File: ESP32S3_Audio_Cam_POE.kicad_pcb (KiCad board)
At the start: 4 copper layers, 109.2 x 129.5 mm, 398 parts, among them J1 Connector, USB-TYPE-C-16P, J10 Conn_01x02, J11 Conn_01x02, J12 Conn_01x02, J13 Conn_01x02, J14 Conn_01x02, J15 Conn_01x02, J16 Conn_01x02, J17 Conn_01x02, J18 Conn_01x02, J19 Conn_01x02, J2 Connector, USB-TYPE-C-16P, J3 Conn_01x02, J4 Conn_01x02, J5 Conn_01x03, J6 Conn_01x03, J7 Conn_01x03, J8 Conn_01x03, J9 HC-RJ45-055-4_8P8C_Shielded, Q1 AO3401A, Q2 AO3401A, Q3 AO3401A, Q4 AO3401A, Q5 AO3401A, Q6 AO3401A, Q7 AO3401A, Q8 AO3401A, T1 H1102NLT, U1 TLV62568DBVR, U10 W25Q128JVSIQ, U11 TM1637, U12 DS18B20U(UMW), U13 W25Q128JVSIQ, U14 DP9900M-5V, U15 MAX98357AETE+T, U16 ICS-43434, U17 ICS-43434, U18 AXP2101, U2 MT9221CT-06BR5, U3 USBLC6-2SC6, U4 USBLC6-2SC6, U5 XC6206-1.5NR, U6 XC6206-2.8V, U7 ESP32-S3, U8 ESP32-S3, U9 W5500, X1 X322525MOB4SI, Y1 40MHz, 15pF, Y2 40MHz, 15pF, Y3 32.768KHz

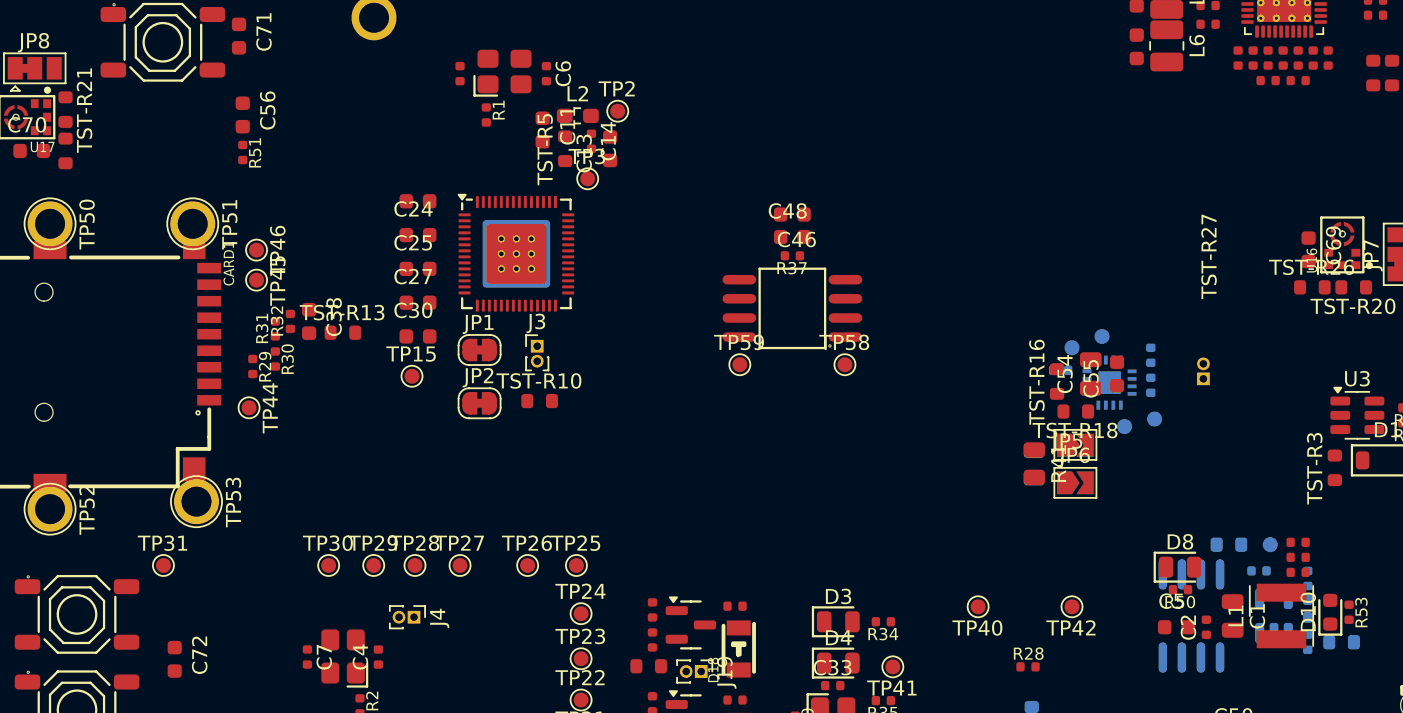
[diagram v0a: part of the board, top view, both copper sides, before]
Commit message: DRAFT added mic jack.
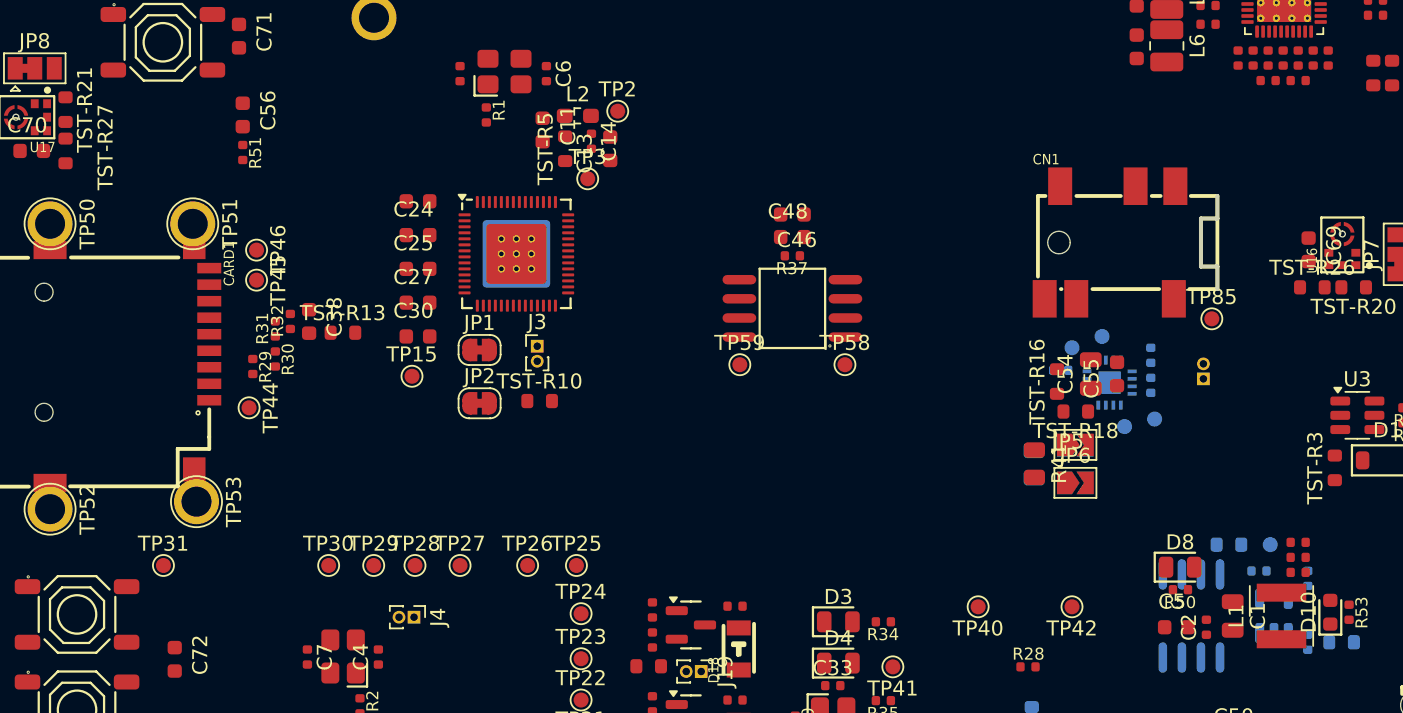
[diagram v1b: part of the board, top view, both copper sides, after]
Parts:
- removed the R8 at (133.4, 113.9)
- added CN1: PJ-316C-6A, JLCPCB:SMD_3.5mm_Audio_Connectors_(Headphones)_C707223, F.Cu at (120.2, 89.5)
- added TP85: TestPoint, TestPoint:TestPoint_Pad_D1.0mm, F.Cu at (127.0, 94.6)
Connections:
- C66 pad 2: Net-(J10-Pin_1) -> /SPK.OutN
- C67 pad 1: Net-(J10-Pin_2) -> /SPK.OutP
- J10 pad 1: Net-(J10-Pin_1) -> /SPK.OutPS
- J10 pad 2: Net-(J10-Pin_2) -> /SPK.OutN
- U15 pad 10: Net-(J10-Pin_1) -> /SPK.OutN
- U15 pad 9: Net-(J10-Pin_2) -> /SPK.OutP

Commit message: Draft Misc changes, layout still needs a lot of work.
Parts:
- added TP100: TestPoint, Connector_PinHeader_1.00mm:PinHeader_1x01_P1.00mm_Vertical, F.Cu at (71.8, 66.3)
- added TP101: TestPoint, Connector_PinHeader_1.00mm:PinHeader_1x01_P1.00mm_Vertical, F.Cu at (72.9, 66.3)
- added TP102: TestPoint, Connector_PinHeader_1.00mm:PinHeader_1x01_P1.00mm_Vertical, F.Cu at (74.1, 65.8)
- added TP103: TestPoint, Connector_PinHeader_1.00mm:PinHeader_1x01_P1.00mm_Vertical, F.Cu at (75.1, 65.8)
- added TP104: TestPoint, Connector_PinHeader_1.00mm:PinHeader_1x01_P1.00mm_Vertical, F.Cu at (76.2, 65.5)
- added TP105: TestPoint, Connector_PinHeader_1.00mm:PinHeader_1x01_P1.00mm_Vertical, F.Cu at (77.3, 65.5)
- added TP106: TestPoint, Connector_PinHeader_1.00mm:PinHeader_1x01_P1.00mm_Vertical, F.Cu at (66.4, 65.0)
- added TP107: TestPoint, Connector_PinHeader_1.00mm:PinHeader_1x01_P1.00mm_Vertical, F.Cu at (65.3, 65.0)
- added TP108: TestPoint, Connector_PinHeader_1.00mm:PinHeader_1x01_P1.00mm_Vertical, F.Cu at (68.6, 64.4)
- added TP109: TestPoint, Connector_PinHeader_1.00mm:PinHeader_1x01_P1.00mm_Vertical, F.Cu at (67.5, 64.4)
- added TP110: TestPoint, Connector_PinHeader_1.00mm:PinHeader_1x01_P1.00mm_Vertical, F.Cu at (70.8, 63.9)
- added TP111: TestPoint, Connector_PinHeader_1.00mm:PinHeader_1x01_P1.00mm_Vertical, F.Cu at (69.8, 63.9)
- added TP112: TestPoint, Connector_PinHeader_1.00mm:PinHeader_1x01_P1.00mm_Vertical, F.Cu at (73.0, 63.4)
- added TP113: TestPoint, Connector_PinHeader_1.00mm:PinHeader_1x01_P1.00mm_Vertical, F.Cu at (71.9, 63.4)
- added TP114: TestPoint, Connector_PinHeader_1.00mm:PinHeader_1x01_P1.00mm_Vertical, F.Cu at (75.1, 62.9)
- added TP115: TestPoint, Connector_PinHeader_1.00mm:PinHeader_1x01_P1.00mm_Vertical, F.Cu at (74.1, 62.9)
- added TP116: TestPoint, Connector_PinHeader_1.00mm:PinHeader_1x01_P1.00mm_Vertical, F.Cu at (77.3, 62.4)
- added TP117: TestPoint, Connector_PinHeader_1.00mm:PinHeader_1x01_P1.00mm_Vertical, F.Cu at (76.3, 62.4)
- added TP118: TestPoint, Connector_PinHeader_1.00mm:PinHeader_1x01_P1.00mm_Vertical, F.Cu at (66.5, 61.8)
- added TP119: TestPoint, Connector_PinHeader_1.00mm:PinHeader_1x01_P1.00mm_Vertical, F.Cu at (65.5, 61.8)
- added TP120: TestPoint, Connector_PinHeader_1.00mm:PinHeader_1x01_P1.00mm_Vertical, F.Cu at (68.6, 61.3)
- added TP121: TestPoint, Connector_PinHeader_1.00mm:PinHeader_1x01_P1.00mm_Vertical, F.Cu at (67.6, 61.3)
- added TP122: TestPoint, Connector_PinHeader_1.00mm:PinHeader_1x01_P1.00mm_Vertical, F.Cu at (70.8, 60.8)
- added TP123: TestPoint, Connector_PinHeader_1.00mm:PinHeader_1x01_P1.00mm_Vertical, F.Cu at (69.8, 60.8)
- added TP124: TestPoint, Connector_PinHeader_1.00mm:PinHeader_1x01_P1.00mm_Vertical, F.Cu at (73.0, 60.3)
- added TP125: TestPoint, Connector_PinHeader_1.00mm:PinHeader_1x01_P1.00mm_Vertical, F.Cu at (71.9, 60.3)
- added TP126: TestPoint, Connector_PinHeader_1.00mm:PinHeader_1x01_P1.00mm_Vertical, F.Cu at (75.1, 59.7)
- added TP127: TestPoint, Connector_PinHeader_1.00mm:PinHeader_1x01_P1.00mm_Vertical, F.Cu at (74.1, 59.7)
- added TP128: TestPoint, Connector_PinHeader_1.00mm:PinHeader_1x01_P1.00mm_Vertical, F.Cu at (77.3, 59.2)
- added TP129: TestPoint, Connector_PinHeader_1.00mm:PinHeader_1x01_P1.00mm_Vertical, F.Cu at (76.3, 59.2)
- added TP86: TestPoint, Connector_PinHeader_1.00mm:PinHeader_1x01_P1.00mm_Vertical, F.Cu at (70.4, 70.2)
- added TP87: TestPoint, Connector_PinHeader_1.00mm:PinHeader_1x01_P1.00mm_Vertical, F.Cu at (69.4, 70.2)
- added TP88: TestPoint, Connector_PinHeader_1.00mm:PinHeader_1x01_P1.00mm_Vertical, F.Cu at (72.7, 69.6)
- added TP89: TestPoint, Connector_PinHeader_1.00mm:PinHeader_1x01_P1.00mm_Vertical, F.Cu at (71.7, 69.6)
- added TP90: TestPoint, Connector_PinHeader_1.00mm:PinHeader_1x01_P1.00mm_Vertical, F.Cu at (74.0, 69.1)
- added TP91: TestPoint, Connector_PinHeader_1.00mm:PinHeader_1x01_P1.00mm_Vertical, F.Cu at (75.0, 69.1)
- added TP92: TestPoint, Connector_PinHeader_1.00mm:PinHeader_1x01_P1.00mm_Vertical, F.Cu at (76.3, 68.5)
- added TP93: TestPoint, Connector_PinHeader_1.00mm:PinHeader_1x01_P1.00mm_Vertical, F.Cu at (77.3, 68.5)
- added TP94: TestPoint, Connector_PinHeader_1.00mm:PinHeader_1x01_P1.00mm_Vertical, F.Cu at (65.0, 67.9)
- added TP95: TestPoint, Connector_PinHeader_1.00mm:PinHeader_1x01_P1.00mm_Vertical, F.Cu at (66.0, 67.9)
- added TP96: TestPoint, Connector_PinHeader_1.00mm:PinHeader_1x01_P1.00mm_Vertical, F.Cu at (67.2, 67.4)
- added TP97: TestPoint, Connector_PinHeader_1.00mm:PinHeader_1x01_P1.00mm_Vertical, F.Cu at (68.3, 67.4)
- added TP98: TestPoint, Connector_PinHeader_1.00mm:PinHeader_1x01_P1.00mm_Vertical, F.Cu at (69.5, 66.9)
- added TP99: TestPoint, Connector_PinHeader_1.00mm:PinHeader_1x01_P1.00mm_Vertical, F.Cu at (70.5, 66.9)
- C11, C13, C14, C3, C6, C69, C70, DISP1, FPC1, JP7, JP8, L2, PB1, PB2, PB3, PB4, PB5, R1, TP2, TP3, TP49, TST-R20, TST-R21, TST-R26, TST-R27, TST-R5, U16, U17, Y1: moved to B.Cu
- C16, C17, C18, C19, C20, C21, C22, C43, C44, C45, C47, Q1, R14, R15, R16, R17, R18, R19, R38, R39, TP11, TP13, TP14, TP47, TP56, TP57, TST-R14, TST-R6, TST-R7, TST-R8, TST-R9, U11, U5, U6: moved to F.Cu
- TP69, TP70, TP71, TP72, TP73, TP74, TP75, TP76, TP77, TP78, TP79, TP80, TP81, TP82, TP83, TP84: footprint TestPoint:TestPoint_Loop_D3.50mm_Drill0.9mm_Beaded -> Connector_PinHeader_1.00mm:PinHeader_1x01_P1.00mm_Vertical
- moved TP82 92.3 mm to (117.2, 67.4)
- moved TP83 88.1 mm to (118.3, 62.1)
- moved TP73 86.0 mm to (118.1, 71.9)
- moved TP77 85.0 mm to (125.0, 72.5)
- moved PB3 84.0 mm to (54.9, 60.8)
- moved TP79 82.5 mm to (122.8, 73.4)
- moved TP74 81.7 mm to (121.0, 73.4)
- moved TP78 81.3 mm to (124.3, 68.6)
- moved TP84 80.2 mm to (124.0, 54.5)
- moved TP80 79.7 mm to (122.1, 68.6)
- moved TP76 79.6 mm to (117.5, 70.2)
- moved TP81 75.0 mm to (134.8, 59.4)
- moved TP72 74.3 mm to (117.5, 69.2)
- moved TP71 73.4 mm to (118.5, 64.2)
- moved TP75 73.3 mm to (126.4, 70.6)
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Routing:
- net Earth: track 0.00 -> 16.9 mm, vias 0 -> 4
- net /CAM.PWDN: track 0.00 -> 14.2 mm, vias 0 -> 1
- net /CAM.RST: track 0.00 -> 14.1 mm
- net /CAM.D7: track 0.00 -> 13.7 mm
- net /CAM.D4: track 0.00 -> 13.5 mm
- net /CAM.VSYNC: track 0.00 -> 11.7 mm
- net /CAM.MCLK: track 0.00 -> 11.3 mm
- net /CAM.D0: track 0.00 -> 11.3 mm
- net /CAM.D6: track 0.00 -> 9.17 mm
- net /CAM.D3: track 0.00 -> 9.11 mm
- net +3V3_RF: track 0.00 -> 8.43 mm, vias 0 -> 1
- net +2V8: track 0.00 -> 7.54 mm
- net /CAM.SDA: track 0.00 -> 7.34 mm
- net /CAM.HREF: track 0.00 -> 7.08 mm
- net /CAM.D1: track 0.00 -> 6.94 mm
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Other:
- outline, holes or cut-outs redrawn

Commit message: Draft misc layout, layout still needs a lot of work
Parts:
- C59, C65, R4, R5: moved to F.Cu
- D1, D2, J1, J2, R10, R11, R12, R13, TST-R3, TST-R4, U3, U4: moved to B.Cu
- moved R40 13.7 mm to (112.8, 90.8), turned to 0 degrees
- moved R41 13.7 mm to (112.8, 90.8), turned to 180 degrees
- moved JP3 13.6 mm to (111.6, 93.5), turned to -90 degrees
- moved JP6 13.6 mm to (111.6, 93.5), turned to -90 degrees
- moved JP4 10.3 mm to (114.1, 93.5), turned to -90 degrees
- moved JP5 10.2 mm to (114.1, 93.5), turned to -90 degrees
- moved CN1 9.66 mm to (127.6, 95.8), turned to -90 degrees
- moved TP85 9.16 mm to (122.5, 102.6), turned to -90 degrees
- moved J10 8.65 mm to (118.5, 102.0), turned to -90 degrees
- moved TP67 7.79 mm to (115.8, 98.8), turned to 0 degrees
- moved TP66 7.72 mm to (115.3, 96.8), turned to 0 degrees
- moved TST-R18 7.44 mm to (116.3, 93.5), turned to 90 degrees
- moved TST-R16 6.71 mm to (118.3, 92.3), turned to 0 degrees
- moved R43 5.90 mm to (119.1, 92.5), turned to -90 degrees
- moved TST-R3 5.60 mm to (147.4, 146.9), turned to 180 degrees
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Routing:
- net /USB_D+: track 0.00 -> 97.5 mm, vias 0 -> 1
- net /USB_D-: track 0.00 -> 96.7 mm, vias 0 -> 1
- net Net-(J14-Pin_1): track 0.00 -> 78.1 mm, vias 0 -> 1
- net Earth: track 16.9 -> 75.6 mm, vias 4 -> 23
- net /2USB_D+: track 0.00 -> 43.0 mm, vias 0 -> 1
- net /2USB_D-: track 0.00 -> 42.3 mm, vias 0 -> 1
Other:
- board size 109.2 x 129.5 mm -> 109.3 x 129.7 mm
